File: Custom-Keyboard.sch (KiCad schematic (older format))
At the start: 14 parts

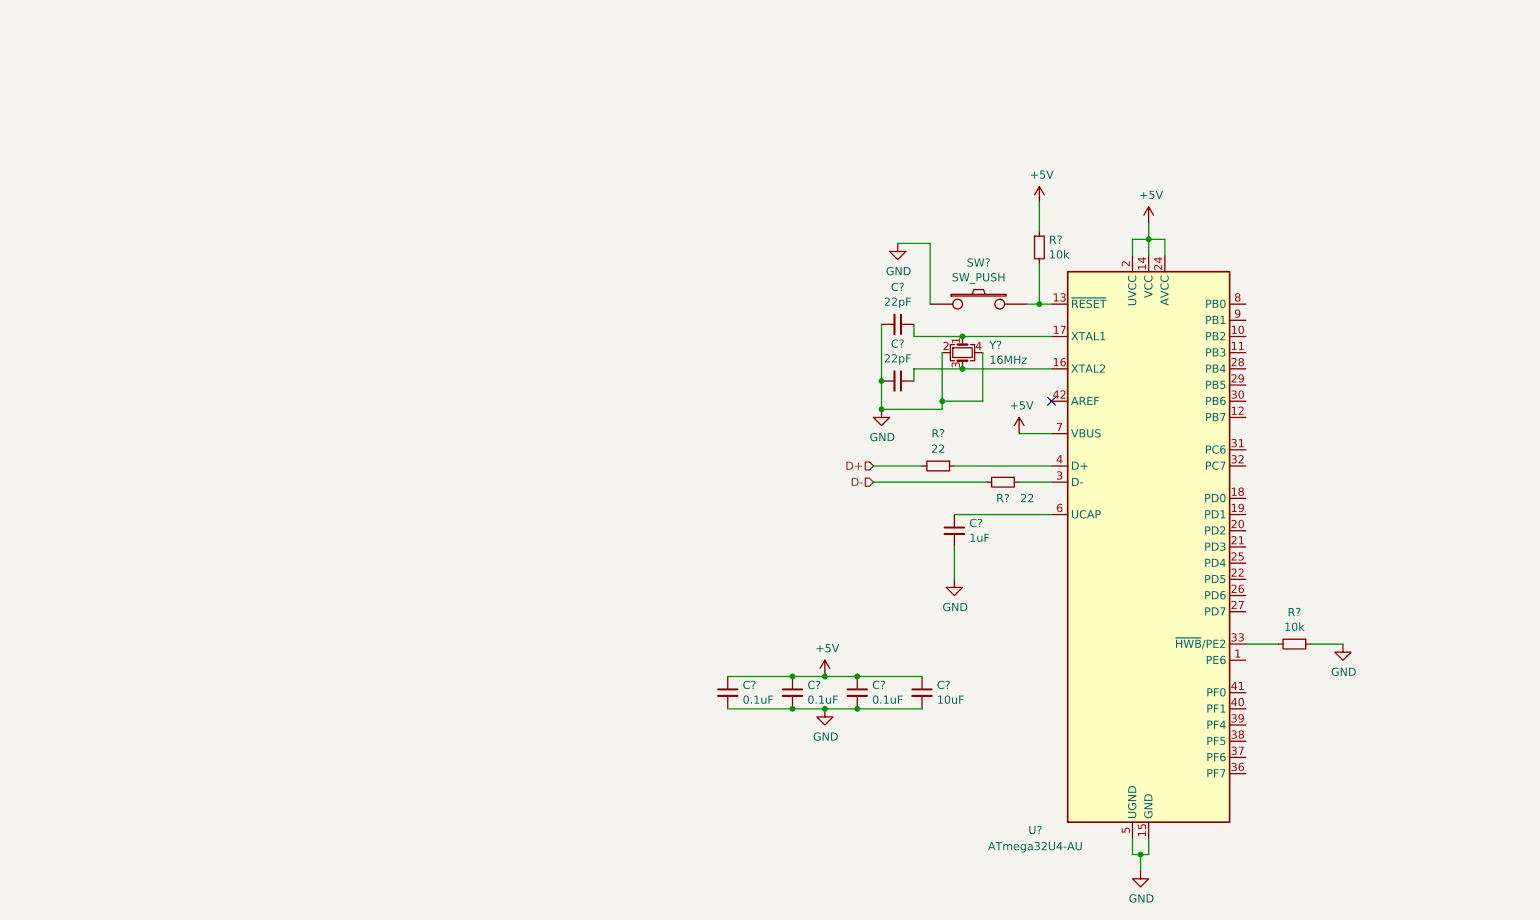
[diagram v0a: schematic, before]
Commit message: Number Pad+Arrow Keys
Added the number pad plus the arrow keys to the schematic. This actually gives me an idea to do a sort of modular add on to 60%s to convert them to southpaw layouts in a single case.
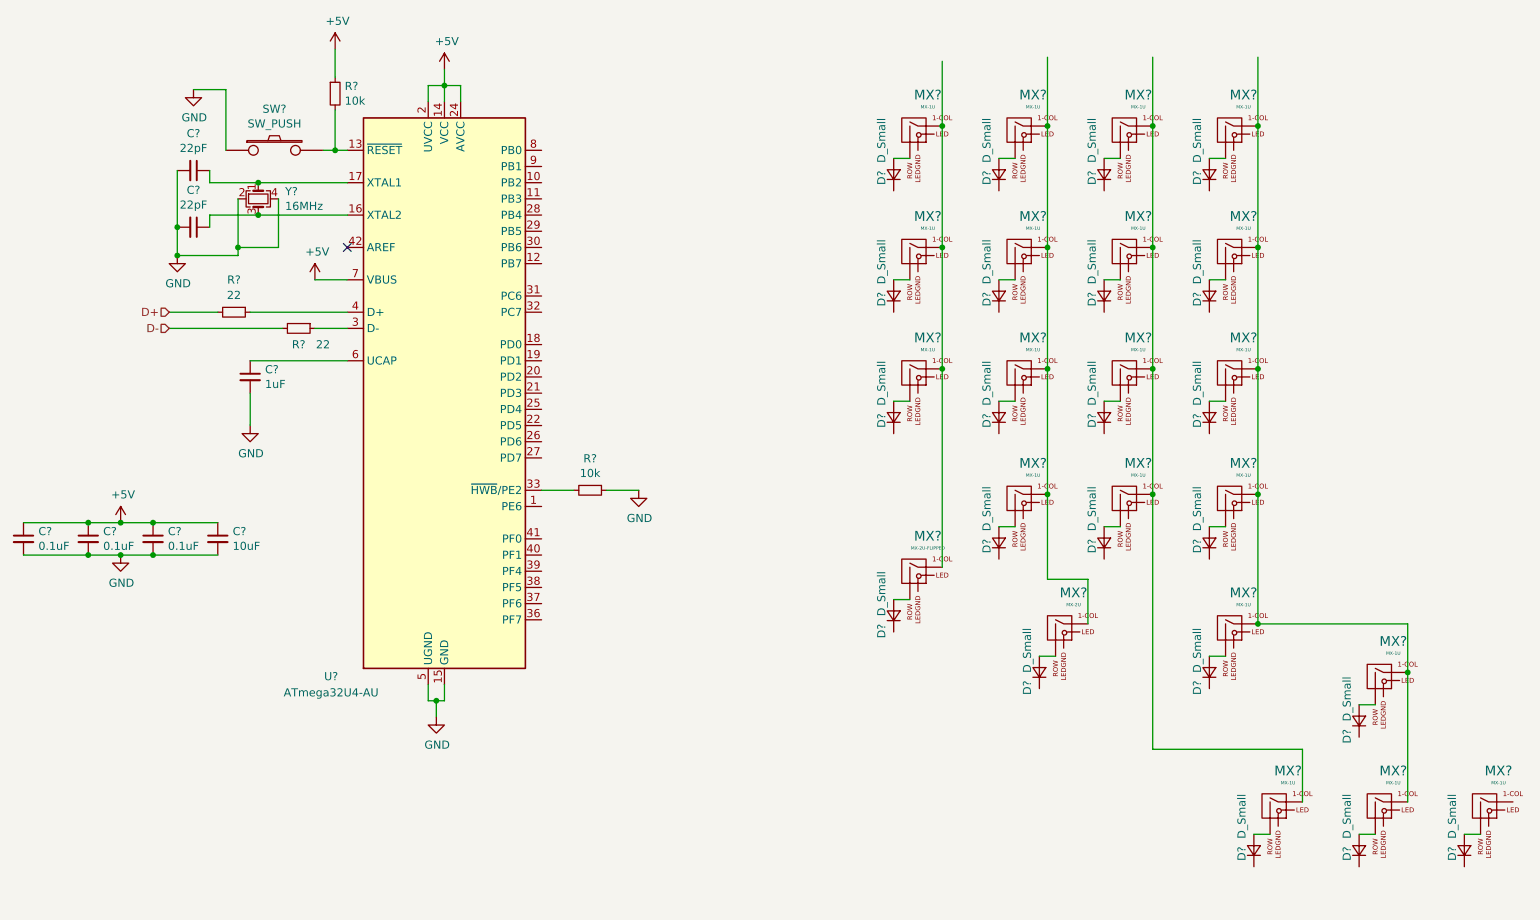
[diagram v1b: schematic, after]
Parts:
- added D? (x22): D_Small, symbol Device:D_Small
- added MX? (x20): MX-1U, symbol MX_Alps_Hybrids:MX-1U
- added MX?: MX-2U-FLIPPED, symbol MX_Alps_Hybrids:MX-2U-FLIPPED
- added MX?: MX-2U, symbol MX_Alps_Hybrids:MX-2U
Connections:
- wire segments 47 -> 95
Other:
- moved on the sheet: C?, R?, SW?, U?, Y?

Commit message: Switch Matrix
Added the full Switch Matrix with Global Labels, with no connections to the Micro-Controller yet.
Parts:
- added D? (x64): D_Small, symbol Device:D_Small
- added MX? (x50): MX-1U, symbol MX_Alps_Hybrids:MX-1U
- added MX? (x2): MX-1.5U, symbol MX_Alps_Hybrids:MX-1.5U
- added MX?: MX-2U, symbol MX_Alps_Hybrids:MX-2U
- added MX?: MX-1.75U, symbol MX_Alps_Hybrids:MX-1.75U
- added MX? (x2): MX-2.25U, symbol MX_Alps_Hybrids:MX-2.25U
- added MX?: MX-2.75U, symbol MX_Alps_Hybrids:MX-2.75U
- added MX? (x6): MX-1.25U, symbol MX_Alps_Hybrids:MX-1.25U
- added MX?: MX-6.25U, symbol MX_Alps_Hybrids:MX-6.25U
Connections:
- net labels added: Col1, Col10, Col11, Col12, Col13, Col14, Col15, Col16, Col17, Col18, Col19, Col2, Col3, Col4, Col5, Col6, Col7, Col8, Col9, Row1, Row2, Row3, Row4, Row5
- wire segments 95 -> 304
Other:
- moved on the sheet: D?, MX?

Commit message: Mini-USB Schematic/Footprints
Added the schematic for the Mini-USB connector, and also mapped them all to Footprints.
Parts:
- added F1: 500mA, Fuse:Fuse_1206_3216Metric_Pad1.42x1.75mm_HandSolder, symbol Device:Polyfuse_Small
- added USB1: Molex-0548190589, random-keyboard-parts:Molex-0548190589, symbol random-keyboard-parts:Molex-0548190589
- AKEY1, BKEY1, CBRAC1, CKEY1, CLN1, CMMA1, EQUALS1, ESC1, FIVE1, FIVE2, FKEY1, FOUR1, FOUR2, FSLSH1, GKEY1, HKEY1, IKEY1, JKEY1, KKEY1, LEFT1, LKEY1, MACRO1, MACRO2, MACRO3, MACRO4, MINUS1, MINUS2, MKEY1, MULT1, NINE1, NINE2, NKEY1, NUM1, OBRAC1, OKEY1, ONE1, ONE2, PER1, PKEY1, PLUS1, QKEY1, QUT1, RGHT1, RKEY1, SEVEN1, SEVEN2, SIX1, SIX2, SKEY1, THREE1, THREE2, TILDE1, TKEY1, TWO1, TWO2, UKEY1, UP1, VKEY1, WKEY1, XKEY1, YKEY1, ZERO2, ZKEY1: renamed from MX?; footprint (none) -> MX_Alps_Hybrid:MX-1U
- ALT1, CTRL1, FN1, LOWER1, RAISE1, WIN1: renamed from MX?; footprint (none) -> MX_Alps_Hybrid:MX-1.25U
- BACK1, ZERO1: renamed from MX?; footprint (none) -> MX_Alps_Hybrid:MX-2U
- BSLSH1, TAB1: renamed from MX?; footprint (none) -> MX_Alps_Hybrid:MX-1.5U
- C1, C2, C3, C4, C5, C6, C7: renamed from C?; footprint (none) -> Capacitor_SMD:C_0805_2012Metric
- CAPS1: renamed from MX?; footprint (none) -> MX_Alps_Hybrid:MX-1.75U
- D1, D10, D11, D12, D13, D14, D15, D16, D17, D18, D19, D2, D20, D21, D22, D23, D24, D25, D26, D27, D28, D29, D3, D30, D31, D32, D33, D34, D35, D36, D37, D38, D39, D4, D40, D41, D42, D43, D44, D45, D46, D47, D48, D49, D5, D50, D51, D52, D53, D54, D55, D56, D57, D58, D59, D6, D60, D61, D62, D63, D64, D65, D66, D67, D68, D69, D7, D70, D71, D72, D73, D74, D75, D76, D77, D78, D79, D8, D80, D81, D82, D83, D84, D85, D86, D9: renamed from D?; footprint (none) -> Diode_SMD:D_SOD-123
- DEL1, DIV1, DKEY1, DOWN1, EIGHT1, EIGHT2, EKEY1: renamed from MX?; footprint (none) -> MX_Alps_Hybrid:MX-1.75U-NoLED
- ENTER1: renamed from MX?; footprint (none) -> MX_Alps_Hybrid:MX-2U-FLIPPED
- ENTER2, SHIFT1: renamed from MX?; footprint (none) -> MX_Alps_Hybrid:MX-2.25U
- R1, R2, R3, R4: renamed from R?; footprint (none) -> Resistor_SMD:R_0805_2012Metric
- SHIFT2: renamed from MX?; footprint (none) -> MX_Alps_Hybrid:MX-2.75U
- SPC1: renamed from MX?; footprint (none) -> MX_Alps_Hybrid:MX-6.25U
- SW1: renamed from SW?; footprint (none) -> random-keyboard-parts:SKQG-1155865
- U1: renamed from U?; footprint Package_QFP:TQFP-44_10x10mm_P0.8mm -> Keebio-Parts:ATMEGA32U4-AU
- Y1: renamed from Y?; footprint (none) -> Crystal:Crystal_SMD_3225-4Pin_3.2x2.5mm
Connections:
- net +5V: now also F1.1
- net D+: now also USB1.3 (D+)
- net D-: now also USB1.4 (D-)
- net GND: now also USB1.1 (GND)
- new net VCC: F1.2, USB1.5 (VBUS)
- no-connect marks 1 -> 3

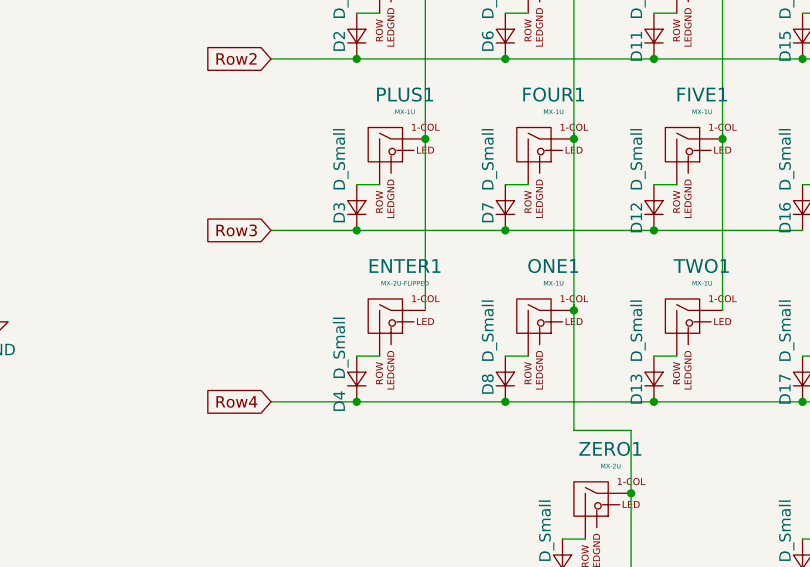
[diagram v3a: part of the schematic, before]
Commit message: Components Placed onto PCB, no routing
Placed all the components on to the PCB. have not done the routing yet. Using Mini-USB for now, because I haven't yet learned USB-C.
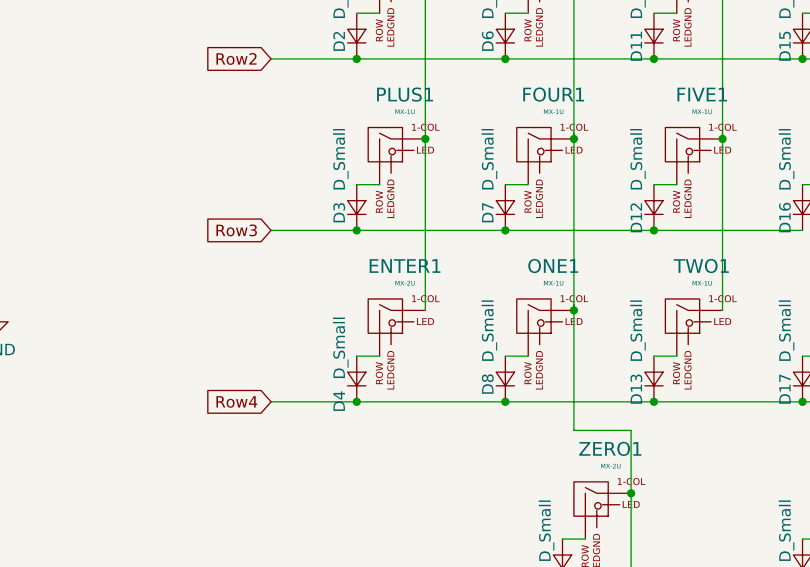
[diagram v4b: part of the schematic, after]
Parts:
- removed ENTER1: MX-2U-FLIPPED, MX_Alps_Hybrid:MX-2U-FLIPPED, symbol MX_Alps_Hybrids:MX-2U-FLIPPED
- added ENTER1: MX-2U, symbol MX_Alps_Hybrids:MX-2U
- DEL1, DIV1, DKEY1, DOWN1, EIGHT1, EIGHT2, EKEY1: footprint MX_Alps_Hybrid:MX-1.75U-NoLED -> MX_Alps_Hybrid:MX-1U
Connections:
- net Col1: now also ENTER1.1 (COL)
- net at D4.2 (A): now also ENTER1.2 (ROW)
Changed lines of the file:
@@
 F 0 "DIV1" H 7336 1592 60  0000 C CNN
 F 1 "MX-1U" H 7336 1518 20  0000 C CNN
-F 2 "MX_Alps_Hybrid:MX-1.75U-NoLED" H 7225 1350 60  0001 C CNN
+F 2 "MX_Alps_Hybrid:MX-1U" H 7225 1350 60  0001 C CNN
 F 3 "" H 7225 1350 60  0001 C CNN
 	1    7250 1375
@@
 F 0 "EIGHT1" H 7986 2342 60  0000 C CNN
 F 1 "MX-1U" H 7986 2268 20  0000 C CNN
-F 2 "MX_Alps_Hybrid:MX-1.75U-NoLED" H 7875 2100 60  0001 C CNN
+F 2 "MX_Alps_Hybrid:MX-1U" H 7875 2100 60  0001 C CNN
 F 3 "" H 7875 2100 60  0001 C CNN
 	1    7900 2125
@@
 	8425 3800 8525 3800
 $Comp
-L MX_Alps_Hybrids:MX-2U-FLIPPED ENTER1
-U 1 1 5C98031C
-P 6600 3625
-F 0 "ENTER1" H 6686 3842 60  0000 C CNN
-F 1 "MX-2U-FLIPPED" H 6686 3768 20  0000 C CNN
-F 2 "MX_Alps_Hybrid:MX-2U-FLIPPED" H 6575 3600 60  0001 C CNN
-F 3 "" H 6575 3600 60  0001 C CNN
-	1    6600 3625
-	1    0    0    -1
-$EndComp
-$Comp
 L MX_Alps_Hybrids:MX-2U ZERO1
 U 1 1 5C980428
@@
 F 0 "DEL1" H 8636 4642 60  0000 C CNN
 F 1 "MX-1U" H 8636 4568 20  0000 C CNN
-F 2 "MX_Alps_Hybrid:MX-1.75U-NoLED" H 8525 4400 60  0001 C CNN
+F 2 "MX_Alps_Hybrid:MX-1U" H 8525 4400 60  0001 C CNN
 F 3 "" H 8525 4400 60  0001 C CNN
 	1    8550 4425
@@
 F 0 "DOWN1" H 9586 5442 60  0000 C CNN
 F 1 "MX-1U" H 9586 5368 20  0000 C CNN
-F 2 "MX_Alps_Hybrid:MX-1.75U-NoLED" H 9475 5200 60  0001 C CNN
+F 2 "MX_Alps_Hybrid:MX-1U" H 9475 5200 60  0001 C CNN
 F 3 "" H 9475 5200 60  0001 C CNN
 	1    9500 5225
@@
 F 0 "EIGHT2" H 15486 1592 60  0000 C CNN
 F 1 "MX-1U" H 15486 1518 20  0000 C CNN
-F 2 "MX_Alps_Hybrid:MX-1.75U-NoLED" H 15375 1350 60  0001 C CNN
+F 2 "MX_Alps_Hybrid:MX-1U" H 15375 1350 60  0001 C CNN
 F 3 "" H 15375 1350 60  0001 C CNN
 	1    15400 1375
@@
 F 0 "EKEY1" H 12261 2342 60  0000 C CNN
 F 1 "MX-1U" H 12261 2268 20  0000 C CNN
-F 2 "MX_Alps_Hybrid:MX-1.75U-NoLED" H 12150 2100 60  0001 C CNN
+F 2 "MX_Alps_Hybrid:MX-1U" H 12150 2100 60  0001 C CNN
 F 3 "" H 12150 2100 60  0001 C CNN
 	1    12175 2125
@@
 F 0 "DKEY1" H 12261 3092 60  0000 C CNN
 F 1 "MX-1U" H 12261 3018 20  0000 C CNN
-F 2 "MX_Alps_Hybrid:MX-1.75U-NoLED" H 12150 2850 60  0001 C CNN
+F 2 "MX_Alps_Hybrid:MX-1U" H 12150 2850 60  0001 C CNN
 F 3 "" H 12150 2850 60  0001 C CNN
 	1    12175 2875
@@
 Text GLabel 2400 6800 2    50   Input ~ 0
 D+
+$Comp
+L MX_Alps_Hybrids:MX-2U ENTER1
+U 1 1 5D7DE43B
+P 6600 3625
+F 0 "ENTER1" H 6686 3842 60  0000 C CNN
+F 1 "MX-2U" H 6686 3768 20  0000 C CNN
+F 2 "" H 6575 3600 60  0001 C CNN
+F 3 "" H 6575 3600 60  0001 C CNN
+	1    6600 3625
+	1    0    0    -1
+$EndComp
 $EndSCHEMATC

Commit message: Routing
All components routed and connected to the MCU.
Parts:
- ENTER1: footprint (none) -> MX_Alps_Hybrid:MX-2U
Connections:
- net Col1: now also U1.1 (PE6)
- net Col10: now also U1.30 (PB6)
- net Col11: now also U1.31 (PC6)
- net Col12: now also U1.32 (PC7)
- net Col13: now also U1.36 (PF7)
- net Col14: now also U1.37 (PF6)
- net Col15: now also U1.38 (PF5)
- net Col16: now also U1.39 (PF4)
- net Col17: now also U1.40 (PF1)
- net Col18: now also U1.41 (PF0)
- net Col19: now also U1.19 (PD1)
- net Col2: now also U1.8 (PB0)
- net Col3: now also U1.9 (PB1)
- net Col4: now also U1.12 (PB7)
- net Col5: now also U1.25 (PD4)
- net Col6: now also U1.26 (PD6)
- net Col7: now also U1.27 (PD7)
- net Col8: now also U1.28 (PB4)
- net Col9: now also U1.29 (PB5)
- net Row1: now also U1.18 (PD0)
- net Row2: now also U1.20 (PD2)
- net Row3: now also D25.1 (K), D30.1 (K), D35.1 (K), D40.1 (K), D44.1 (K), D48.1 (K), D52.1 (K), D57.1 (K), D61.1 (K), D65.1 (K), D69.1 (K), D74.1 (K), D81.1 (K), D85.1 (K), U1.21 (PD3)
- net Row4: now also U1.22 (PD5)
- net Row5: now also U1.10 (PB2)
- net Row6: now reaches U1.11 (PB3)
- net Row6: now also D19.1 (K), D21.1 (K), D22.1 (K)
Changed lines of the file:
@@
 F 0 "ENTER1" H 6686 3842 60  0000 C CNN
 F 1 "MX-2U" H 6686 3768 20  0000 C CNN
-F 2 "" H 6575 3600 60  0001 C CNN
+F 2 "MX_Alps_Hybrid:MX-2U" H 6575 3600 60  0001 C CNN
 F 3 "" H 6575 3600 60  0001 C CNN
 	1    6600 3625
 	1    0    0    -1
 $EndComp
+Wire Wire Line
+	8825 5600 6100 5600
+Connection ~ 8825 5600
+Text GLabel 6100 5600 0    50   Input ~ 0
+Row6
+Wire Wire Line
+	8425 3250 10100 3250
+Connection ~ 8425 3250
+Wire Wire Line
+	10100 3250 10750 3250
+Connection ~ 10100 3250
+Connection ~ 10750 3250
+Wire Wire Line
+	10750 3250 11400 3250
+Connection ~ 11400 3250
+Wire Wire Line
+	11400 3250 12050 3250
+Connection ~ 12050 3250
+Wire Wire Line
+	12050 3250 12675 3250
+Connection ~ 12675 3250
+Wire Wire Line
+	12675 3250 13325 3250
+Connection ~ 13325 3250
+Wire Wire Line
+	13325 3250 13975 3250
+Connection ~ 13975 3250
+Wire Wire Line
+	13975 3250 14625 3250
+Connection ~ 14625 3250
+Wire Wire Line
+	14625 3250 15275 3250
+Connection ~ 15275 3250
+Wire Wire Line
+	15275 3250 15925 3250
+Connection ~ 15925 3250
+Wire Wire Line
+	15925 3250 16575 3250
+Connection ~ 16575 3250
+Wire Wire Line
+	16575 3250 17225 3250
+Connection ~ 17225 3250
+Wire Wire Line
+	17225 3250 18475 3250
+Connection ~ 18475 3250
+Wire Wire Line
+	18475 3250 19100 3250
+Text GLabel 4300 3100 2    50   Input ~ 0
+Col5
+Text GLabel 4300 3300 2    50   Input ~ 0
+Col6
+Text GLabel 4300 3400 2    50   Input ~ 0
+Col7
+Text GLabel 4300 1900 2    50   Input ~ 0
+Col8
+Text GLabel 4300 2000 2    50   Input ~ 0
+Col9
+Text GLabel 4300 2100 2    50   Input ~ 0
+Col10
+Text GLabel 4300 2400 2    50   Input ~ 0
+Col11
+Text GLabel 4300 2500 2    50   Input ~ 0
+Col12
+Text GLabel 4300 4400 2    50   Input ~ 0
+Col13
+Text GLabel 4300 4300 2    50   Input ~ 0
+Col14
+Text GLabel 4300 4200 2    50   Input ~ 0
+Col15
+Text GLabel 4300 4100 2    50   Input ~ 0
+Col16
+Text GLabel 4300 4000 2    50   Input ~ 0
+Col17
+Text GLabel 4300 3900 2    50   Input ~ 0
+Col18
+Text GLabel 4300 2700 2    50   Input ~ 0
+Row1
+Text GLabel 4300 2800 2    50   Input ~ 0
+Col19
+Text GLabel 4300 2900 2    50   Input ~ 0
+Row2
+Text GLabel 4300 3000 2    50   Input ~ 0
+Row3
+Text GLabel 4300 3200 2    50   Input ~ 0
+Row4
+Text GLabel 4300 1700 2    50   Input ~ 0
+Row5
+Text GLabel 4300 1800 2    50   Input ~ 0
+Row6
+Text GLabel 4300 2200 2    50   Input ~ 0
+Col4
+Text GLabel 4300 1600 2    50   Input ~ 0
+Col3
+Text GLabel 4300 1500 2    50   Input ~ 0
+Col2
+Text GLabel 4300 3700 2    50   Input ~ 0
+Col1
 $EndSCHEMATC

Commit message: Footprint Change - No LEDs
Schematic has LED pads, but since I don't intend to add LEDs to the keyboard just yet, I changed the footprints to not have any. Don't want there to be any confusion.
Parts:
- AKEY1, BKEY1, CBRAC1, CKEY1, CLN1, CMMA1, DEL1, DIV1, DKEY1, DOWN1, EIGHT1, EIGHT2, EKEY1, EQUALS1, ESC1, FIVE1, FIVE2, FKEY1, FOUR1, FOUR2, FSLSH1, GKEY1, HKEY1, IKEY1, JKEY1, KKEY1, LEFT1, LKEY1, MACRO1, MACRO2, MACRO3, MACRO4, MINUS1, MINUS2, MKEY1, MULT1, NINE1, NINE2, NKEY1, NUM1, OBRAC1, OKEY1, ONE1, ONE2, PER1, PKEY1, PLUS1, QKEY1, QUT1, RGHT1, RKEY1, SEVEN1, SEVEN2, SIX1, SIX2, SKEY1, THREE1, THREE2, TILDE1, TKEY1, TWO1, TWO2, UKEY1, UP1, VKEY1, WKEY1, XKEY1, YKEY1, ZERO2, ZKEY1: footprint MX_Alps_Hybrid:MX-1U -> MX_Alps_Hybrid:MXOnly-1U-NoLED
- ALT1, CTRL1, FN1, LOWER1, WIN1: footprint MX_Alps_Hybrid:MX-1.25U -> MX_Alps_Hybrid:MXOnly-1.25U-NoLED
- BACK1, ENTER1, ZERO1: footprint MX_Alps_Hybrid:MX-2U -> MX_Alps_Hybrid:MXOnly-2U-NoLED
- BSLSH1, TAB1: footprint MX_Alps_Hybrid:MX-1.5U -> MX_Alps_Hybrid:MXOnly-1.5U-NoLED
- CAPS1: footprint MX_Alps_Hybrid:MX-1.75U -> MX_Alps_Hybrid:MXOnly-1.75U-NoLED
- ENTER2, SHIFT1: footprint MX_Alps_Hybrid:MX-2.25U -> MX_Alps_Hybrid:MXOnly-2.25U-NoLED
- SHIFT2: footprint MX_Alps_Hybrid:MX-2.75U -> MX_Alps_Hybrid:MXOnly-2.75U-NoLED
- SPC1: footprint MX_Alps_Hybrid:MX-6.25U -> MX_Alps_Hybrid:MXOnly-6.25U-NoLED

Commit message: MASSIVE Mess Up fix
Rebuilt the whole repository from a back up because I screwed up pretty badly when testing USB-C.
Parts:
- AKEY1, BKEY1, CBRAC1, CKEY1, CLN1, CMMA1, DEL1, DIV1, DKEY1, DOWN1, EIGHT1, EIGHT2, EKEY1, EQUALS1, ESC1, FIVE1, FIVE2, FKEY1, FOUR1, FOUR2, FSLSH1, GKEY1, HKEY1, IKEY1, JKEY1, KKEY1, LEFT1, LKEY1, MACRO1, MACRO2, MACRO3, MACRO4, MINUS1, MINUS2, MKEY1, MULT1, NINE1, NINE2, NKEY1, NUM1, OBRAC1, OKEY1, ONE1, ONE2, PER1, PKEY1, PLUS1, QKEY1, QUT1, RGHT1, RKEY1, SEVEN1, SEVEN2, SIX1, SIX2, SKEY1, THREE1, THREE2, TILDE1, TKEY1, TWO1, TWO2, UKEY1, UP1, VKEY1, WKEY1, XKEY1, YKEY1, ZERO2, ZKEY1: symbol MX_Alps_Hybrids:MX-1U -> Custom-Keyboard-rescue:MX-1U-MX_Alps_Hybrids
- ALT1, CTRL1, FN1, LOWER1, WIN1: symbol MX_Alps_Hybrids:MX-1.25U -> Custom-Keyboard-rescue:MX-1.25U-MX_Alps_Hybrids
- BACK1, ENTER1, ZERO1: symbol MX_Alps_Hybrids:MX-2U -> Custom-Keyboard-rescue:MX-2U-MX_Alps_Hybrids
- BSLSH1, TAB1: symbol MX_Alps_Hybrids:MX-1.5U -> Custom-Keyboard-rescue:MX-1.5U-MX_Alps_Hybrids
- CAPS1: symbol MX_Alps_Hybrids:MX-1.75U -> Custom-Keyboard-rescue:MX-1.75U-MX_Alps_Hybrids
- ENTER2, SHIFT1: symbol MX_Alps_Hybrids:MX-2.25U -> Custom-Keyboard-rescue:MX-2.25U-MX_Alps_Hybrids
- RAISE1: footprint MX_Alps_Hybrid:MX-1.25U -> MX_Alps_Hybrid:MXOnly-1.25U-NoLED; symbol MX_Alps_Hybrids:MX-1.25U -> Custom-Keyboard-rescue:MX-1.25U-MX_Alps_Hybrids
- SHIFT2: symbol MX_Alps_Hybrids:MX-2.75U -> Custom-Keyboard-rescue:MX-2.75U-MX_Alps_Hybrids
- SPC1: symbol MX_Alps_Hybrids:MX-6.25U -> Custom-Keyboard-rescue:MX-6.25U-MX_Alps_Hybrids
- USB1: symbol random-keyboard-parts:Molex-0548190589 -> Custom-Keyboard-rescue:Molex-0548190589-random-keyboard-parts
